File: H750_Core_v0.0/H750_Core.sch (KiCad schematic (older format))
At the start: 0 parts

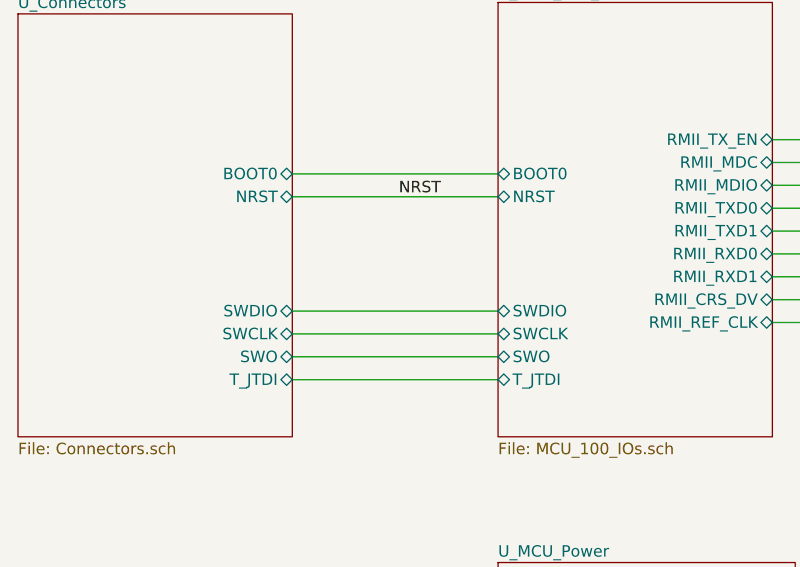
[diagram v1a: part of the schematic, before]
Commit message: 修改编程接口
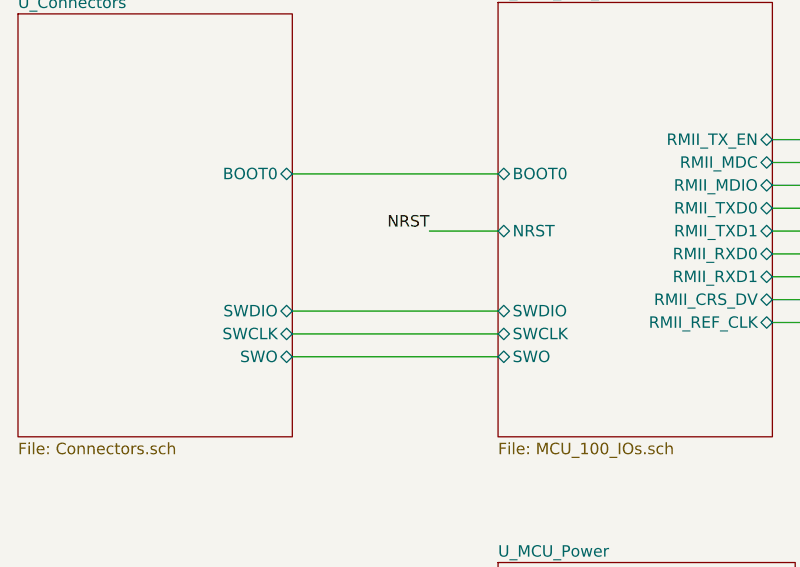
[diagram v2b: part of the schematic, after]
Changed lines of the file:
@@
 EESchema Schematic File Version 4
-LIBS:H750_Core-cache
 EELAYER 30 0
 EELAYER END
@@
 F12 "SWO" B L 4550 3100 50
 F13 "SWCLK" B L 4550 3000 50
-F14 "T_JTDI" B L 4550 3200 50
-F15 "BOOT0" B L 4550 2300 50
-F16 "NRST" B L 4550 2400 50
+F14 "BOOT0" B L 4550 2300 50
+F15 "NRST" B L 4550 2550 50
 $EndSheet
 $Sheet
@@
 F2 "SWDIO" B R 3650 2900 50
 F3 "SWCLK" B R 3650 3000 50
-F4 "T_JTDI" B R 3650 3200 50
-F5 "SWO" B R 3650 3100 50
-F6 "BOOT0" B R 3650 2300 50
-F7 "NRST" B R 3650 2400 50
+F4 "SWO" B R 3650 3100 50
+F5 "BOOT0" B R 3650 2300 50
 $EndSheet
 $Sheet
@@
 Text Label 8050 2250 0    50   ~ 0
 NRST
-Text Label 4300 2400 2    50   ~ 0
-NRST
 $Sheet
 S 6500 3600 1050 850
@@
 F1 "External_Memory.sch" 50
 $EndSheet
-Wire Wire Line
-	3650 3200 4550 3200
 Wire Wire Line
 	4550 3100 3650 3100
@@
 Wire Wire Line
 	3650 2300 4550 2300
+Text Label 4250 2550 2    50   ~ 0
+NRST
 Wire Wire Line
-	3650 2400 4550 2400
+	4250 2550 4550 2550
 $EndSCHEMATC
